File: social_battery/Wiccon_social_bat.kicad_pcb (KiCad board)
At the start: 2 copper layers, 84.5 x 43.3 mm, 20 parts, among them J1 SAO, SW1 Change, U1 CH32V003

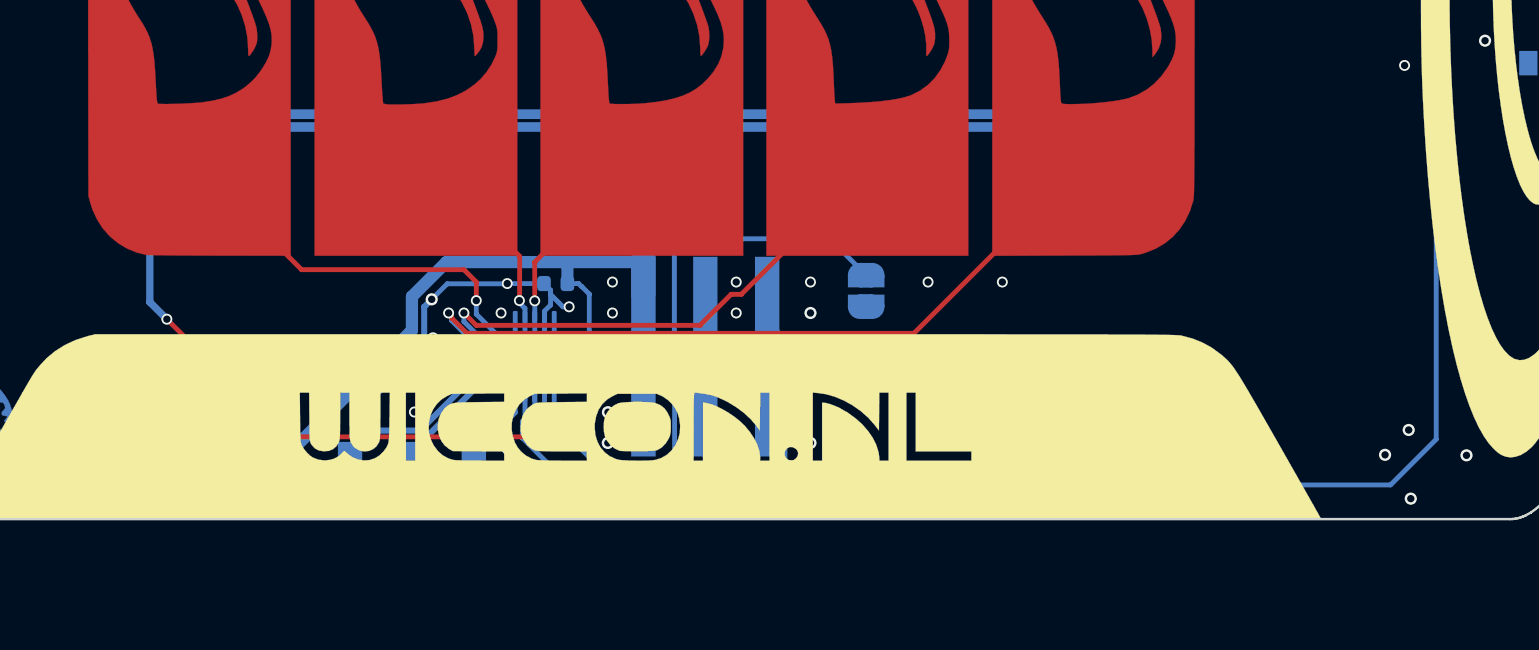
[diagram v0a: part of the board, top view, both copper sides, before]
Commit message: Separate SAO IO1 from LED control on social battery, add firmware
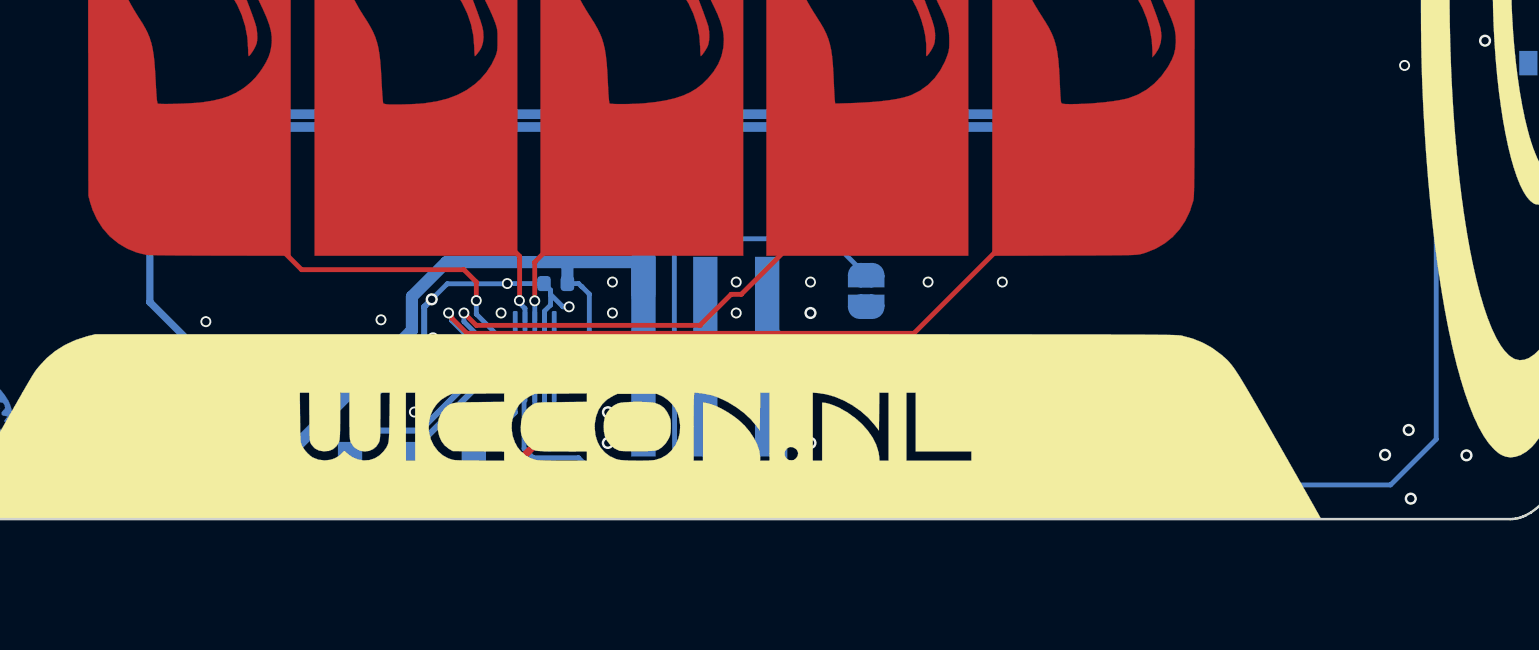
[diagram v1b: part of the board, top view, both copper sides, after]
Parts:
- moved R1 0.78 mm to (-5.97, 18.6), turned to 180 degrees
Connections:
- net Net-(U1-PC6) renamed LED
- LED1 pad 1: GPIO1 -> Net-(LED1-DIN)
- R1 pad 2: GPIO1 -> Net-(LED1-DIN)
- U1 pad 12: unconnected-(U1-PC5-Pad12) -> GPIO1
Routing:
- net Net-(LED1-DIN): track 0.00 -> 27.7 mm, vias 0 -> 2
- net GPIO1: track 43.4 -> 18.7 mm, vias 2 -> 0
- net LED: track 1.46 -> 3.16 mm
- net GND: vias 37 -> 40
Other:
- board text added: "M"
- board text removed: "A"

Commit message: Added text to back silkscreen
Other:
- board text added: "v1.0"
